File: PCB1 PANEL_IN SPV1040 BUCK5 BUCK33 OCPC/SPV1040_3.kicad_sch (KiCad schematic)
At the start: 14 parts, among them J2 SOLAR, U2 SPV1040TTR

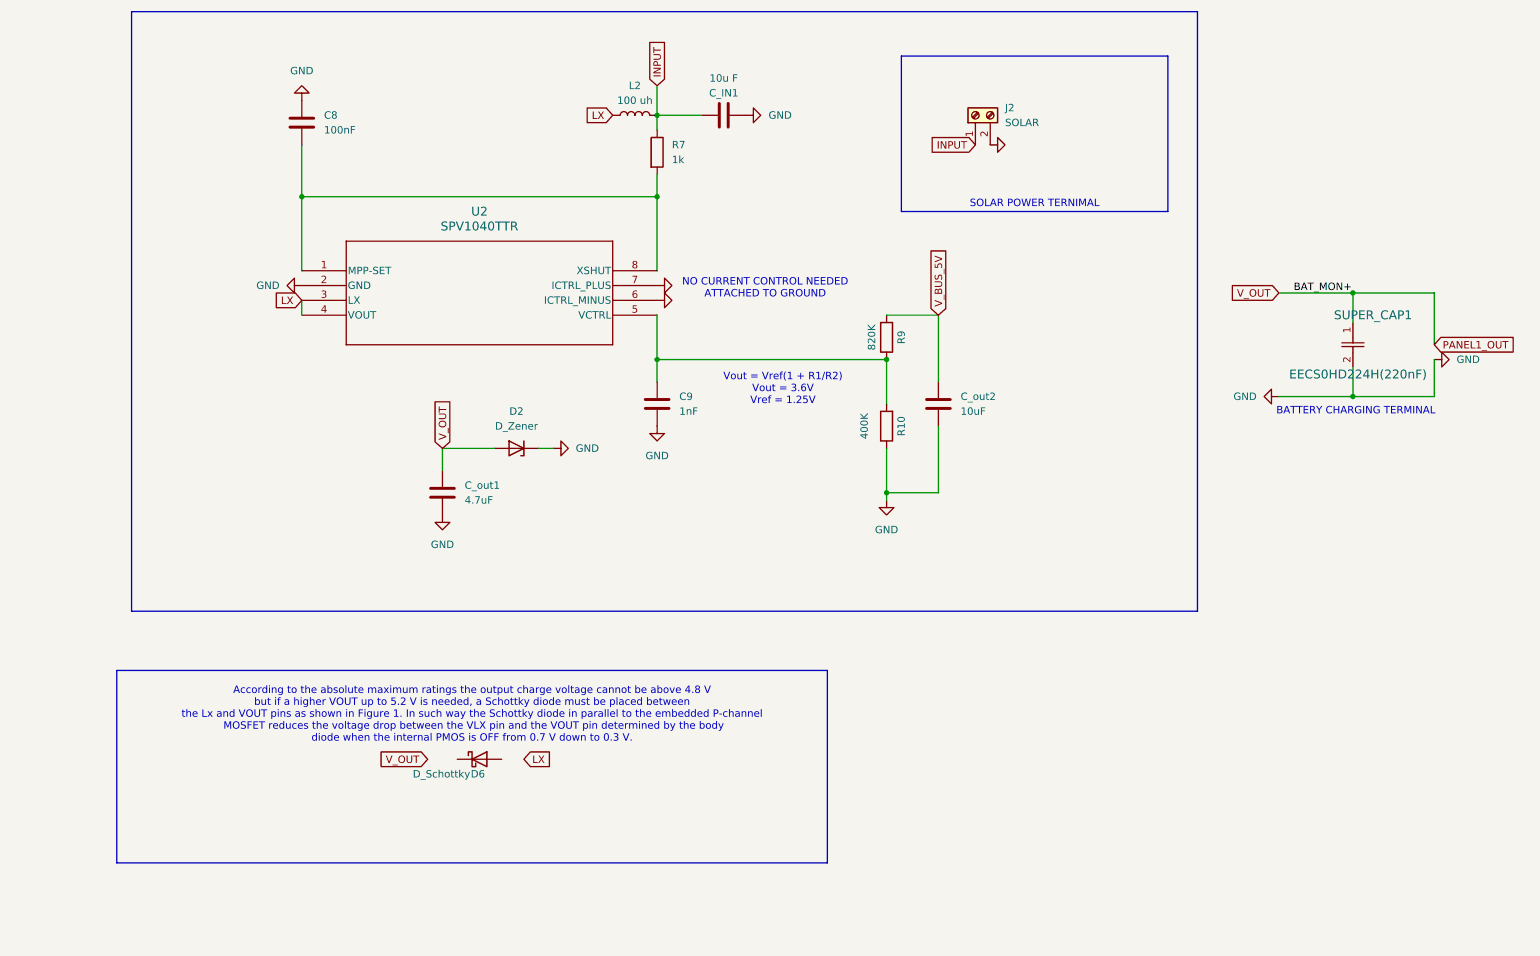
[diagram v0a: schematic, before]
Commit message: Changes
Added bucks from old work
and copied SPV
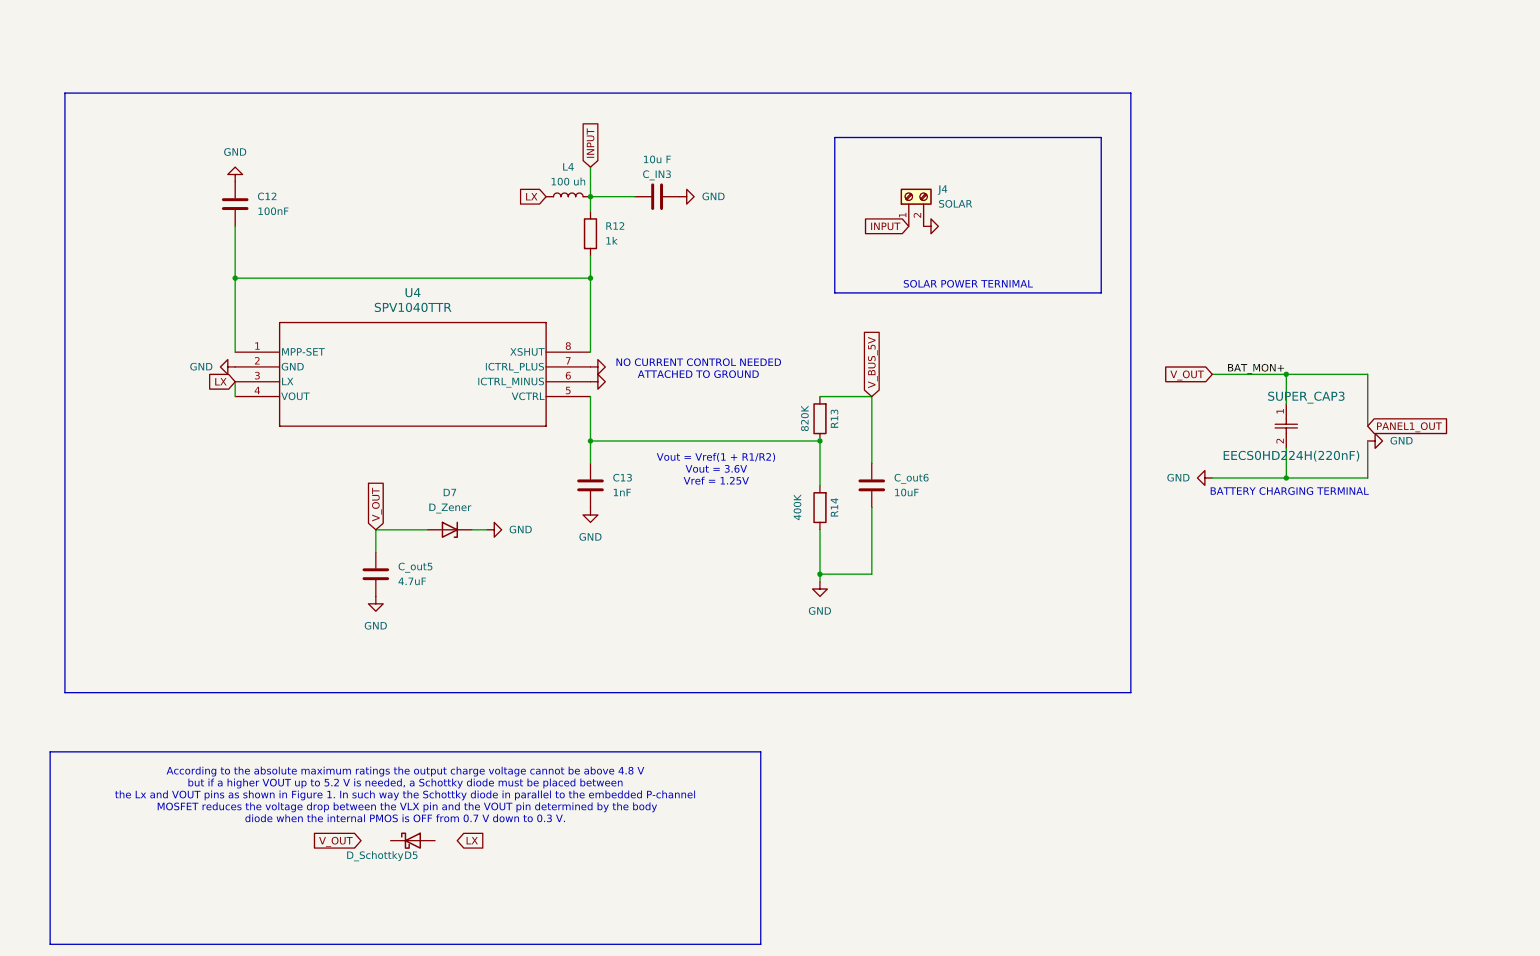
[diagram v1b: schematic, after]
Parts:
- removed C8: 100nF, Capacitor_SMD:C_0603_1608Metric, symbol Device:C
- removed C9: 1nF, Capacitor_SMD:C_0603_1608Metric, symbol Device:C
- removed C_IN1: 10u F, Capacitor_SMD:C_0603_1608Metric, symbol Device:C
- removed C_out1: 4.7uF, Capacitor_SMD:C_0603_1608Metric, symbol Device:C
- removed C_out2: 10uF, Capacitor_SMD:C_0603_1608Metric, symbol Device:C
- removed D2: D_Zener, Diode_SMD:D_1210_3225Metric, symbol Device:D_Zener
- removed D6: D_Schottky, symbol Device:D_Schottky
- removed J2: SOLAR, TerminalBlock_Phoenix:TerminalBlock_Phoenix_PT-1,5-2-5.0-H_1x02_P5.00mm_Horizontal, symbol Connector:Screw_Terminal_01x02
- removed L2: 100 uh, Inductor_SMD:L_Coilcraft_XAL6060-XXX, symbol Device:L
- removed R10: 400K, Resistor_SMD:R_0603_1608Metric, symbol Device:R
- removed R7: 1k, Resistor_SMD:R_0603_1608Metric, symbol Device:R
- removed R9: 820K, Resistor_SMD:R_0603_1608Metric, symbol Device:R
- removed SUPER_CAP1: EECS0HD224H(220nF), SPV1040T:CAP_EECS0_H_PAN, symbol 2024-06-08_06-57-05:super_capacitor
- removed U2: SPV1040TTR, SPV1040:SOP65P640X120-8N, symbol 2024-06-07_14-27-39:SPV1040TTR
- added C12: 100nF, Capacitor_SMD:C_0603_1608Metric, symbol Device:C
- added C13: 1nF, Capacitor_SMD:C_0603_1608Metric, symbol Device:C
- added C_IN3: 10u F, Capacitor_SMD:C_0603_1608Metric, symbol Device:C
- added C_out5: 4.7uF, Capacitor_SMD:C_0603_1608Metric, symbol Device:C
- added C_out6: 10uF, Capacitor_SMD:C_0603_1608Metric, symbol Device:C
- added D5: D_Schottky, symbol Device:D_Schottky
- added D7: D_Zener, Diode_SMD:D_1210_3225Metric, symbol Device:D_Zener
- added J4: SOLAR, TerminalBlock_Phoenix:TerminalBlock_Phoenix_PT-1,5-2-5.0-H_1x02_P5.00mm_Horizontal, symbol Connector:Screw_Terminal_01x02
- added L4: 100 uh, Inductor_SMD:L_Coilcraft_XAL6060-XXX, symbol Device:L
- added R12: 1k, Resistor_SMD:R_0603_1608Metric, symbol Device:R
- added R13: 820K, Resistor_SMD:R_0603_1608Metric, symbol Device:R
- added R14: 400K, Resistor_SMD:R_0603_1608Metric, symbol Device:R
- added SUPER_CAP3: EECS0HD224H(220nF), SPV1040T:CAP_EECS0_H_PAN, symbol 2024-06-08_06-57-05:super_capacitor
- added U4: SPV1040TTR, SPV1040:SOP65P640X120-8N, symbol 2024-06-07_14-27-39:SPV1040TTR
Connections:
- net GND: now also C12.1, C13.2, C_IN3.2, C_out5.1, C_out6.2, D7.1 (K), J4.2 (Pin_2), R14.1, SUPER_CAP3.2, U4.2 (GND), U4.6 (ICTRL_MINUS), U4.7 (ICTRL_PLUS)
- net INPUT: now also C_IN3.1, J4.1 (Pin_1), L4.2, R12.1
- net LX: now also L4.1, U4.3 (LX), U4.4 (VOUT)
- net PANEL1_OUT: now also C_out5.2, D7.2 (A), SUPER_CAP3.1
- net V_BUS_5V: now also C_out6.1, R13.2
- new net: C12.2, R12.2, U4.1 (MPP-SET), U4.8 (XSHUT)
- new net: C13.1, R13.1, R14.2, U4.5 (VCTRL)
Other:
- company: TEAM ANANT -> (none)
- title: SOLAR CHARGER -> (none)

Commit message: w
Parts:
- removed D7: D_Zener, Diode_SMD:D_1210_3225Metric, symbol Device:D_Zener
- added CR2: SMM4F5.0A-TR, CR_F5.0A-TR_STM, symbol SMM4F5:SMM4F5.0A-TR
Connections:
- net GND: now also CR2.1
- net PANEL1_OUT: now also CR2.2
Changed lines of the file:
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@@
-	(wire
-		(pts
-			(xy 93.98 109.22) (xy 96.52 109.22)
-		)
-		(stroke
-			(width 0)
-			(type default)
-		)
-	)
 	(wire
 		(pts
@@
 	)
 	(symbol
-		(lib_id "Device:D_Zener")
-		(at 90.17 109.22 180)
-		(unit 1)
-		(exclude_from_sim no)
-		(in_bom yes)
-		(on_board yes)
-		(dnp no)
-		(fields_autoplaced yes)
-		(property "Reference" "D7"
-			(at 90.17 102.87 0)
-			(effects
-				(font
-					(size 1.27 1.27)
-				)
-			)
-		)
-		(property "Value" "D_Zener"
-			(at 90.17 105.41 0)
-			(effects
-				(font
-					(size 1.27 1.27)
-				)
-			)
-		)
-		(property "Footprint" "Diode_SMD:D_1210_3225Metric"
-			(at 90.17 109.22 0)
-			(effects
-				(font
-					(size 1.27 1.27)
-				)
-				(hide yes)
-			)
-		)
-		(property "Datasheet" "~"
-			(at 90.17 109.22 0)
-			(effects
-				(font
-					(size 1.27 1.27)
-				)
-				(hide yes)
-			)
-		)
-		(property "Description" "Zener diode"
-			(at 90.17 109.22 0)
-			(effects
-				(font
-					(size 1.27 1.27)
-				)
-				(hide yes)
-			)
-		)
-		(pin "2"
-		)
-		(pin "1"
-		)
-		(instances
-			(project "PCB1 PANEL_IN SPV1040 BUCK5 BUCK33 OCPC"
-				(path "/494c9d9f-6b33-4248-a813-27ffaaa929bd/e998d71e-4e87-4975-a251-a83701b03c75"
-					(reference "D7")
-					(unit 1)
-				)
-			)
-		)
-	)
-	(symbol
 		(lib_id "power:GND")
 		(at 114.3 81.28 90)
@@
 					(unit 1)
 				)
+			)
+		)
+	)
+	(symbol
+		(lib_id "SMM4F5:SMM4F5.0A-TR")
+		(at 86.36 109.22 0)
+		(unit 1)
+		(exclude_from_sim no)
+		(in_bom yes)
+		(on_board yes)
+		(dnp no)
+		(fields_autoplaced yes)
+		(property "Reference" "CR2"
+			(at 91.44 102.87 0)
+			(effects
+				(font
+					(size 1.524 1.524)
+				)
+			)
+		)
+		(property "Value" "SMM4F5.0A-TR"
+			(at 91.44 105.41 0)
+			(effects
+				(font
+					(size 1.524 1.524)
+				)
+			)
+		)
+		(property "Footprint" "CR_F5.0A-TR_STM"
+			(at 86.36 109.22 0)
+			(effects
+				(font
+					(size 1.27 1.27)
+					(italic yes)
+				)
+				(hide yes)
+			)
+		)
+		(property "Datasheet" "SMM4F5.0A-TR"
+			(at 86.36 109.22 0)
+			(effects
+				(font
+					(size 1.27 1.27)
+					(italic yes)
+				)
+				(hide yes)
+			)
+		)
+		(property "Description" ""
+			(at 86.36 109.22 0)
+			(effects
+				(font
+					(size 1.27 1.27)
+				)
+				(hide yes)
+			)
+		)
+		(pin "1"
+		)
+		(pin "2"
+		)
+		(instances
+			(project "PCB1 PANEL_IN SPV1040 BUCK5 BUCK33 OCPC"
+				(path "/494c9d9f-6b33-4248-a813-27ffaaa929bd/e998d71e-4e87-4975-a251-a83701b03c75"
+					(reference "CR2")
+					(unit 1)
+				)

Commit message: Relabeling according to standards
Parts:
- D1601: renamed from CR2; footprint CR_F5.0A-TR_STM -> (none)
- renumbered C12 to C1601, C_out5 to C1602, C13 to C1603, C_out6 to C1604, C_IN3 to C1605, D5 to D1602, J4 to J1601, L4 to L1601, R12 to R1601, R13 to R1602, R14 to R1603, SUPER_CAP3 to SUPER_CAP1601, U4 to U1601
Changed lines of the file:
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@@
 		(dnp no)
 		(fields_autoplaced yes)
-		(property "Reference" "C_out5"
+		(property "Reference" "C1602"
 			(at 81.28 115.5699 0)
 			(effects
@@
 			(project "PCB1 PANEL_IN SPV1040 BUCK5 BUCK33 OCPC"
 				(path "/494c9d9f-6b33-4248-a813-27ffaaa929bd/e998d71e-4e87-4975-a251-a83701b03c75"
-					(reference "C_out5")
+					(reference "C1602")
 					(unit 1)
 				)
@@
 		(dnp no)
 		(fields_autoplaced yes)
-		(property "Reference" "C12"
+		(property "Reference" "C1601"
 			(at 57.15 52.0699 0)
 			(effects
@@
 			(project "PCB1 PANEL_IN SPV1040 BUCK5 BUCK33 OCPC"
 				(path "/494c9d9f-6b33-4248-a813-27ffaaa929bd/e998d71e-4e87-4975-a251-a83701b03c75"
-					(reference "C12")
+					(reference "C1601")
 					(unit 1)
 				)
@@
 		(dnp no)
 		(fields_autoplaced yes)
-		(property "Reference" "C13"
+		(property "Reference" "C1603"
 			(at 118.11 100.3299 0)
 			(effects
@@
 			(project "PCB1 PANEL_IN SPV1040 BUCK5 BUCK33 OCPC"
 				(path "/494c9d9f-6b33-4248-a813-27ffaaa929bd/e998d71e-4e87-4975-a251-a83701b03c75"
-					(reference "C13")
+					(reference "C1603")
 					(unit 1)
 				)
@@
 		(on_board yes)
 		(dnp no)
-		(property "Reference" "SUPER_CAP3"
+		(property "Reference" "SUPER_CAP1601"
 			(at 243.84 86.36 90)
 			(effects
@@
 			(project "PCB1 PANEL_IN SPV1040 BUCK5 BUCK33 OCPC"
 				(path "/494c9d9f-6b33-4248-a813-27ffaaa929bd/e998d71e-4e87-4975-a251-a83701b03c75"
-					(reference "SUPER_CAP3")
+					(reference "SUPER_CAP1601")
 					(unit 1)
 				)
@@
 		(on_board yes)
 		(dnp no)
-		(property "Reference" "C_IN3"
+		(property "Reference" "C1605"
 			(at 125.73 48.26 90)
 			(effects
@@
 			(project "PCB1 PANEL_IN SPV1040 BUCK5 BUCK33 OCPC"
 				(path "/494c9d9f-6b33-4248-a813-27ffaaa929bd/e998d71e-4e87-4975-a251-a83701b03c75"
-					(reference "C_IN3")
+					(reference "C1605")
 					(unit 1)
 				)
@@
 		(dnp no)
 		(fields_autoplaced yes)
-		(property "Reference" "L4"
+		(property "Reference" "L1601"
 			(at 110.49 46.99 90)
 			(effects
@@
 			(project "PCB1 PANEL_IN SPV1040 BUCK5 BUCK33 OCPC"
 				(path "/494c9d9f-6b33-4248-a813-27ffaaa929bd/e998d71e-4e87-4975-a251-a83701b03c75"
-					(reference "L4")
+					(reference "L1601")
 					(unit 1)
 				)
@@
 		(dnp no)
 		(fields_autoplaced yes)
-		(property "Reference" "C_out6"
+		(property "Reference" "C1604"
 			(at 166.37 100.3299 0)
 			(effects
@@
 			(project "PCB1 PANEL_IN SPV1040 BUCK5 BUCK33 OCPC"
 				(path "/494c9d9f-6b33-4248-a813-27ffaaa929bd/e998d71e-4e87-4975-a251-a83701b03c75"
-					(reference "C_out6")
+					(reference "C1604")
 					(unit 1)
 				)
@@
 		(on_board yes)
 		(dnp no)
-		(property "Reference" "R13"
+		(property "Reference" "R1602"
 			(at 156.21 90.17 90)
 			(effects
@@
 			(project "PCB1 PANEL_IN SPV1040 BUCK5 BUCK33 OCPC"
 				(path "/494c9d9f-6b33-4248-a813-27ffaaa929bd/e998d71e-4e87-4975-a251-a83701b03c75"
-					(reference "R13")
+					(reference "R1602")
 					(unit 1)
 				)
@@
 		(dnp no)
 		(fields_autoplaced yes)
-		(property "Reference" "J4"
+		(property "Reference" "J1601"
 			(at 173.99 50.7999 90)
 			(effects
@@
 			(project "PCB1 PANEL_IN SPV1040 BUCK5 BUCK33 OCPC"
 				(path "/494c9d9f-6b33-4248-a813-27ffaaa929bd/e998d71e-4e87-4975-a251-a83701b03c75"
-					(reference "J4")
+					(reference "J1601")
 					(unit 1)
 				)
@@
 		(dnp no)
 		(fields_autoplaced yes)
-		(property "Reference" "R12"
+		(property "Reference" "R1601"
 			(at 116.84 57.1499 0)
 			(effects
@@
 			(project "PCB1 PANEL_IN SPV1040 BUCK5 BUCK33 OCPC"
 				(path "/494c9d9f-6b33-4248-a813-27ffaaa929bd/e998d71e-4e87-4975-a251-a83701b03c75"
-					(reference "R12")
+					(reference "R1601")
 					(unit 1)
 				)
@@
 		(dnp no)
 		(fields_autoplaced yes)
-		(property "Reference" "CR2"
+		(property "Reference" "D1601"
 			(at 91.44 102.87 0)
 			(effects
@@
 			)
 		)
-		(property "Footprint" "CR_F5.0A-TR_STM"
+		(property "Footprint" ""
 			(at 86.36 109.22 0)
 			(effects
@@
 			(project "PCB1 PANEL_IN SPV1040 BUCK5 BUCK33 OCPC"
 				(path "/494c9d9f-6b33-4248-a813-27ffaaa929bd/e998d71e-4e87-4975-a251-a83701b03c75"
-					(reference "CR2")
+					(reference "D1601")
 					(unit 1)
 				)
@@
 		(on_board yes)
 		(dnp no)
-		(property "Reference" "D5"
+		(property "Reference" "D1602"
 			(at 84.7726 165.1 0)
 			(effects
@@
 			(project "PCB1 PANEL_IN SPV1040 BUCK5 BUCK33 OCPC"
 				(path "/494c9d9f-6b33-4248-a813-27ffaaa929bd/e998d71e-4e87-4975-a251-a83701b03c75"
-					(reference "D5")
+					(reference "D1602")
 					(unit 1)
 				)
@@
 		(dnp no)
 		(fields_autoplaced yes)
-		(property "Reference" "U4"
+		(property "Reference" "U1601"
 			(at 83.82 68.58 0)
 			(effects
@@
 			(project "PCB1 PANEL_IN SPV1040 BUCK5 BUCK33 OCPC"
 				(path "/494c9d9f-6b33-4248-a813-27ffaaa929bd/e998d71e-4e87-4975-a251-a83701b03c75"
-					(reference "U4")
+					(reference "U1601")
 					(unit 1)
 				)
@@
 		(on_board yes)
 		(dnp no)
-		(property "Reference" "R14"
+		(property "Reference" "R1603"
 			(at 156.21 105.41 90)
 			(effects
@@
 			(project "PCB1 PANEL_IN SPV1040 BUCK5 BUCK33 OCPC"
 				(path "/494c9d9f-6b33-4248-a813-27ffaaa929bd/e998d71e-4e87-4975-a251-a83701b03c75"
-					(reference "R14")
-					(unit 1)
-				)
+					(reference "R1603")
+					(unit 1)
+				)
